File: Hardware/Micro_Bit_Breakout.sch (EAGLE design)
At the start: 11 parts, among them J2 CONN_22_NOSILK, U1 micro:bit

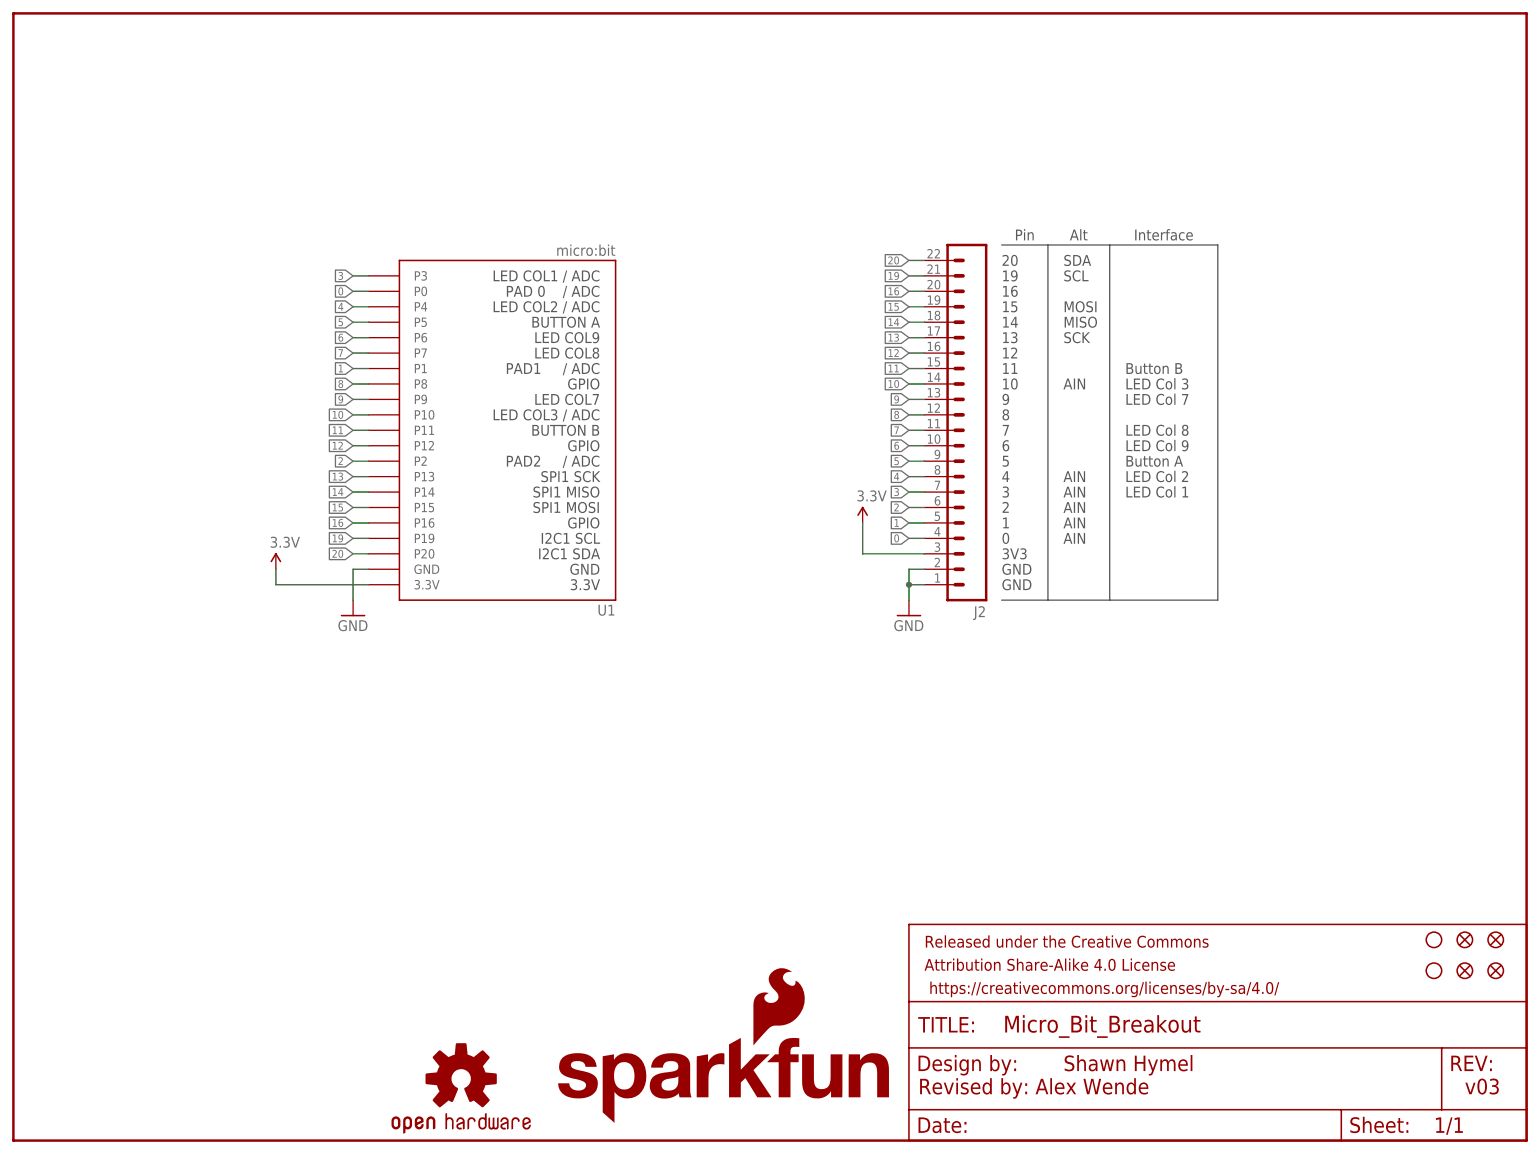
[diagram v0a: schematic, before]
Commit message: Added Qwiic Connectors
Added virtical qwiic connectors
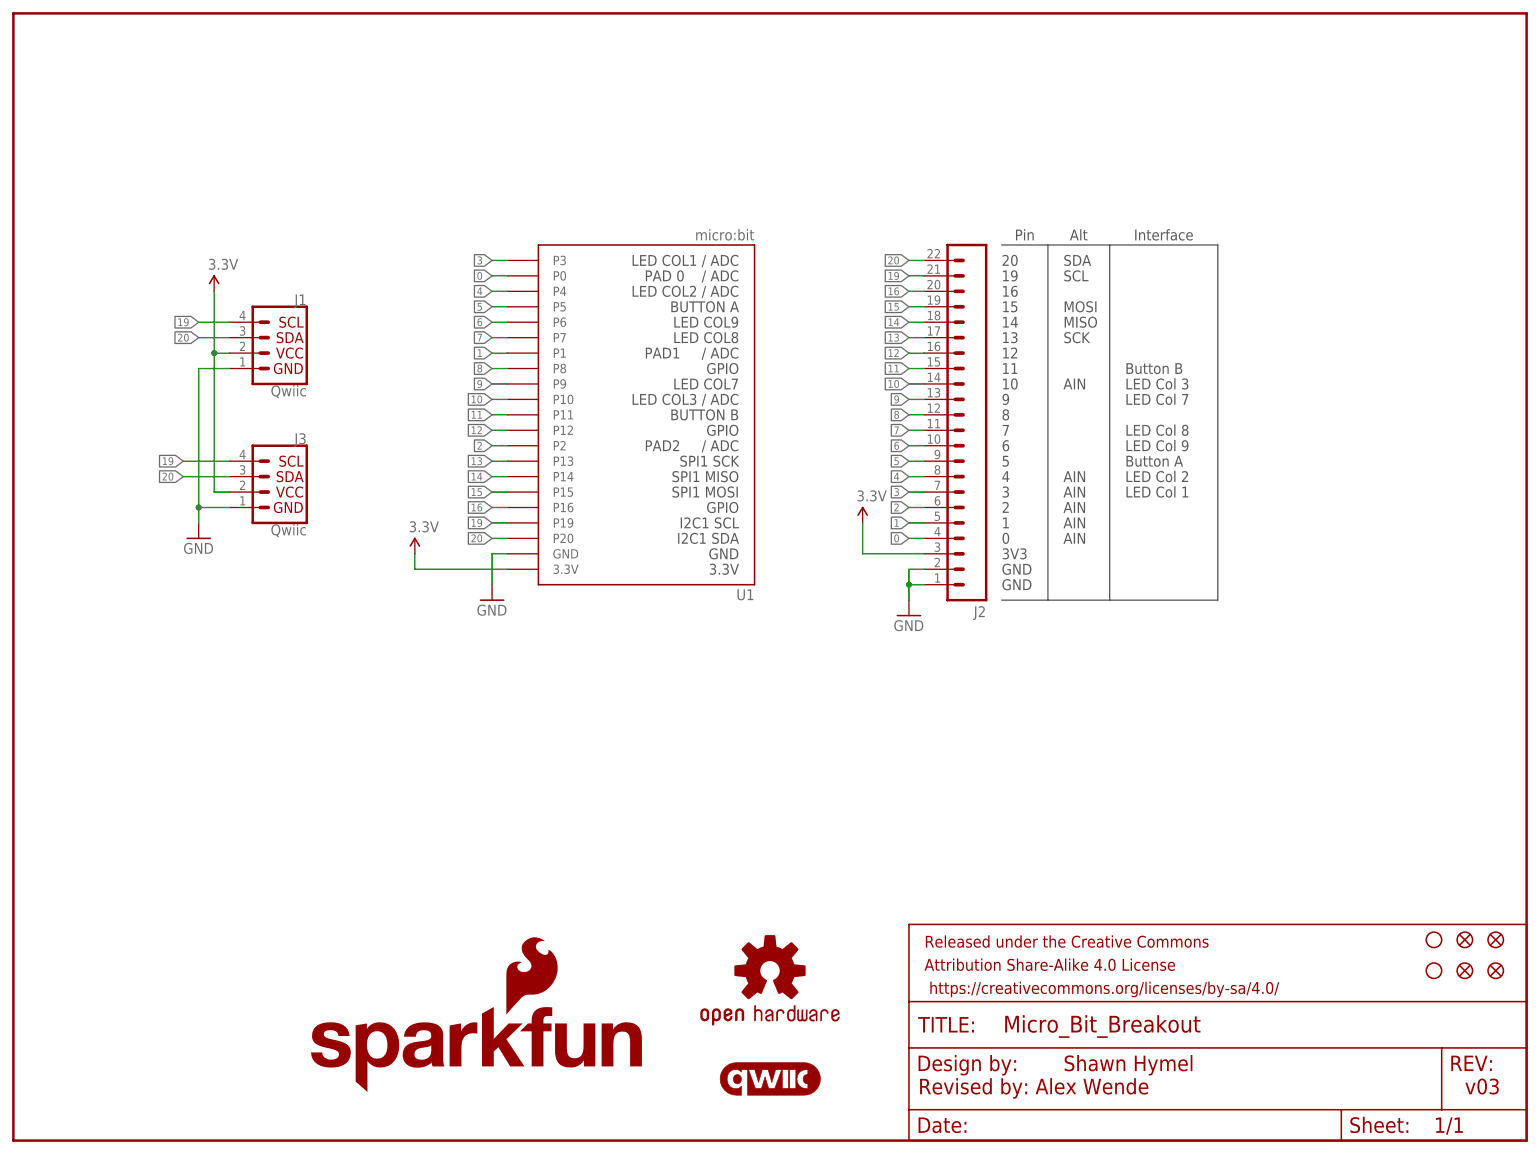
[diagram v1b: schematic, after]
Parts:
- added J1, J3: Qwiic, SparkFun-Connectors:QWIIC_CONNECTOR
- added LOGO1: QWIIC_LOGO_5MM, SparkFun-Aesthetics:QWIIC_LOGO_5MM
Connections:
- net 19: now also J1.4, J3.4
- net 20: now also J1.3, J3.3
- net 3.3V: now also J1.2, J3.2
- net GND: now also J1.1, J3.1
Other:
- moved on the sheet: U1
